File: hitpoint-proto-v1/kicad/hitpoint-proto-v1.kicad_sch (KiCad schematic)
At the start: 22 parts, among them J1 Conn_01x05_Male, J2 Conn_01x06_Female, J3 Conn_01x06_Female, J4 Conn_01x06_Female, J5 Conn_01x06_Female, U1 STM32G030Fx, U2 IRM-H6XXT

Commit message: PCB done so far
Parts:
- added C1: 100nF, Capacitor_SMD:C_0603_1608Metric, symbol Device:C
- renumbered C1 to C2, C2 to C3, C3 to C4, C4 to C5, C5 to C6, C6 to C7
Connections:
- net +3V3: now also J2.1 (Pin_1), J3.1 (Pin_1), J4.1 (Pin_1), J5.1 (Pin_1), C1.1; no longer J2.2 (Pin_2), J3.2 (Pin_2), J4.2 (Pin_2), J5.2 (Pin_2)
- net +5V: now also J2.2 (Pin_2), J3.2 (Pin_2), J4.2 (Pin_2), J5.2 (Pin_2); no longer J2.1 (Pin_1), J3.1 (Pin_1), J4.1 (Pin_1), J5.1 (Pin_1)
- net GND: now also C1.2
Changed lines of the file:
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@@
   (symbol (lib_id "Device:C") (at 137.16 66.04 0) (unit 1)
     (in_bom yes) (on_board yes)
-    (property "Reference" "C3" (id 0) (at 138.43 63.5 0)
+    (property "Reference" "C4" (id 0) (at 138.43 63.5 0)
       (effects (font (size 1.27 1.27)) (justify left))
     )
@@
   (symbol (lib_id "Device:C") (at 30.48 119.38 0) (unit 1)
     (in_bom yes) (on_board yes)
-    (property "Reference" "C1" (id 0) (at 31.75 121.92 0)
-      (effects (font (size 1.27 1.27)) (justify left))
-    )
-    (property "Value" "10uF" (id 1) (at 31.75 124.46 0)
+    (property "Reference" "C2" (id 0) (at 31.75 116.84 0)
+      (effects (font (size 1.27 1.27)) (justify left))
+    )
+    (property "Value" "10uF" (id 1) (at 31.75 121.92 0)
       (effects (font (size 1.27 1.27)) (justify left))
     )
@@
     (pin "6")
   )
-  (symbol (lib_id "power:+5V") (at 193.04 123.19 90) (unit 1)
-    (in_bom yes) (on_board yes)
-    (property "Reference" "#PWR013" (id 0) (at 196.85 123.19 0)
-      (effects (font (size 1.27 1.27)) hide)
-    )
-    (property "Value" "+5V" (id 1) (at 187.96 123.19 90))
-    (property "Footprint" "" (id 2) (at 193.04 123.19 0)
-      (effects (font (size 1.27 1.27)) hide)
-    )
-    (property "Datasheet" "" (id 3) (at 193.04 123.19 0)
-      (effects (font (size 1.27 1.27)) hide)
-    )
-    (pin "1")
-  )
   (symbol (lib_id "LED:WS2812B") (at 86.36 66.04 0) (unit 1)
     (in_bom yes) (on_board yes) (fields_autoplaced)
@@
   (symbol (lib_id "Device:C") (at 152.4 66.04 0) (unit 1)
     (in_bom yes) (on_board yes)
-    (property "Reference" "C5" (id 0) (at 153.67 63.5 0)
+    (property "Reference" "C6" (id 0) (at 153.67 63.5 0)
       (effects (font (size 1.27 1.27)) (justify left))
     )
@@
     (pin "2")
   )
+  (symbol (lib_name "+3V3_1") (lib_id "power:+3V3") (at 193.04 123.19 90) (unit 1)
+    (in_bom yes) (on_board yes) (fields_autoplaced)
+    (property "Reference" "#PWR0101" (id 0) (at 196.85 123.19 0)
+      (effects (font (size 1.27 1.27)) hide)
+    )
+    (property "Value" "+3V3" (id 1) (at 189.23 123.1899 90)
+      (effects (font (size 1.27 1.27)) (justify left))
+    )
+    (property "Footprint" "" (id 2) (at 193.04 123.19 0)
+      (effects (font (size 1.27 1.27)) hide)
+    )
+    (property "Datasheet" "" (id 3) (at 193.04 123.19 0)
+      (effects (font (size 1.27 1.27)) hide)
+    )
+    (pin "1")
+  )
   (symbol (lib_id "Device:C") (at 232.41 66.04 180) (unit 1)
     (in_bom yes) (on_board yes) (fields_autoplaced)
-    (property "Reference" "C6" (id 0) (at 236.22 64.7699 0)
+    (property "Reference" "C7" (id 0) (at 236.22 64.7699 0)
       (effects (font (size 1.27 1.27)) (justify right))
     )
@@
     (pin "2")
   )
-  (symbol (lib_name "+3V3_1") (lib_id "power:+3V3") (at 193.04 120.65 90) (unit 1)
-    (in_bom yes) (on_board yes)
-    (property "Reference" "#PWR012" (id 0) (at 196.85 120.65 0)
-      (effects (font (size 1.27 1.27)) hide)
-    )
-    (property "Value" "+3V3" (id 1) (at 187.96 120.65 90))
-    (property "Footprint" "" (id 2) (at 193.04 120.65 0)
-      (effects (font (size 1.27 1.27)) hide)
-    )
-    (property "Datasheet" "" (id 3) (at 193.04 120.65 0)
-      (effects (font (size 1.27 1.27)) hide)
-    )
-    (pin "1")
-  )
   (symbol (lib_id "Device:C") (at 144.78 66.04 0) (unit 1)
     (in_bom yes) (on_board yes)
-    (property "Reference" "C4" (id 0) (at 146.05 63.5 0)
+    (property "Reference" "C5" (id 0) (at 146.05 63.5 0)
       (effects (font (size 1.27 1.27)) (justify left))
     )
@@
   (symbol (lib_id "Device:C") (at 129.54 66.04 0) (unit 1)
     (in_bom yes) (on_board yes)
-    (property "Reference" "C2" (id 0) (at 130.81 63.5 0)
+    (property "Reference" "C3" (id 0) (at 130.81 63.5 0)
       (effects (font (size 1.27 1.27)) (justify left))
     )
@@
     (pin "6")
   )
+  (symbol (lib_id "power:+5V") (at 193.04 120.65 90) (unit 1)
+    (in_bom yes) (on_board yes) (fields_autoplaced)
+    (property "Reference" "#PWR0102" (id 0) (at 196.85 120.65 0)
+      (effects (font (size 1.27 1.27)) hide)
+    )
+    (property "Value" "+5V" (id 1) (at 189.23 120.6499 90)
+      (effects (font (size 1.27 1.27)) (justify left))
+    )
+    (property "Footprint" "" (id 2) (at 193.04 120.65 0)
+      (effects (font (size 1.27 1.27)) hide)
+    )
+    (property "Datasheet" "" (id 3) (at 193.04 120.65 0)
+      (effects (font (size 1.27 1.27)) hide)
+    )
+    (pin "1")
+  )
   (symbol (lib_id "Jumper:SolderJumper_2_Open") (at 125.73 115.57 90) (unit 1)
     (in_bom yes) (on_board yes)
@@
     )
     (pin "1")
+  )
+  (symbol (lib_id "Device:C") (at 22.86 119.38 0) (unit 1)
+    (in_bom yes) (on_board yes)
+    (property "Reference" "C1" (id 0) (at 24.13 116.84 0)
+      (effects (font (size 1.27 1.27)) (justify left))
+    )
+    (property "Value" "100nF" (id 1) (at 24.13 121.92 0)
+      (effects (font (size 1.27 1.27)) (justify left))
+    )
+    (property "Footprint" "Capacitor_SMD:C_0603_1608Metric" (id 2) (at 23.8252 123.19 0)
+      (effects (font (size 1.27 1.27)) hide)
+    )
+    (property "Datasheet" "~" (id 3) (at 22.86 119.38 0)
+      (effects (font (size 1.27 1.27)) hide)
+    )
+    (pin "1")
+    (pin "2")
   )
   (sheet_instances
@@
       (reference "#PWR011") (unit 1) (value "GND") (footprint "")
     )
-    (path "/b7a976fa-776a-4ab1-b0a2-37f6ebbf77de"
-      (reference "#PWR012") (unit 1) (value "+3V3") (footprint "")
-    )
-    (path "/956b6541-0348-4f73-b296-9061cb0e27ac"
-      (reference "#PWR013") (unit 1) (value "+5V") (footprint "")
-    )
     (path "/003fb1b7-be45-49c5-a590-681af9a34456"
       (reference "#PWR014") (unit 1) (value "GND") (footprint "")
@@
       (reference "#PWR016") (unit 1) (value "GND") (footprint "")
     )
+    (path "/a8c8ab2a-565a-403d-8f11-1f7ad63e290c"
+      (reference "#PWR0101") (unit 1) (value "+3V3") (footprint "")
+    )
+    (path "/d0ea6a16-603e-4cab-913e-14dd7c01c704"
+      (reference "#PWR0102") (unit 1) (value "+5V") (footprint "")
+    )
+    (path "/ee84faa3-67fd-47c1-8473-f69cd565e2c1"
+      (reference "C1") (unit 1) (value "100nF") (footprint "Capacitor_SMD:C_0603_1608Metric")
+    )
     (path "/5d0df2f0-223d-46e6-b5a4-c4a18f51cf9e"
-      (reference "C1") (unit 1) (value "10uF") (footprint "Capacitor_SMD:C_0805_2012Metric")
+      (reference "C2") (unit 1) (value "10uF") (footprint "Capacitor_SMD:C_0805_2012Metric")
     )
     (path "/c0eacd68-7a4c-4235-b140-b3d29b2ecb3e"
-      (reference "C2") (unit 1) (value "100nF") (footprint "Capacitor_SMD:C_0603_1608Metric")
+      (reference "C3") (unit 1) (value "100nF") (footprint "Capacitor_SMD:C_0603_1608Metric")
     )
     (path "/51436e77-e776-4180-9349-cc544ecbe37c"
-      (reference "C3") (unit 1) (value "100nF") (footprint "Capacitor_SMD:C_0603_1608Metric")
+      (reference "C4") (unit 1) (value "100nF") (footprint "Capacitor_SMD:C_0603_1608Metric")
     )
     (path "/bd03bacc-8ae0-415d-ac2b-025d5f175e5f"
-      (reference "C4") (unit 1) (value "100nF") (footprint "Capacitor_SMD:C_0603_1608Metric")
+      (reference "C5") (unit 1) (value "100nF") (footprint "Capacitor_SMD:C_0603_1608Metric")
     )
     (path "/a03d9d9a-4690-420f-a7c2-6d2e45cec7d3"
-      (reference "C5") (unit 1) (value "100nF") (footprint "Capacitor_SMD:C_0603_1608Metric")
+      (reference "C6") (unit 1) (value "100nF") (footprint "Capacitor_SMD:C_0603_1608Metric")
     )
     (path "/b169ee8a-f50b-482f-bd86-29ad5f7cd978"
-      (reference "C6") (unit 1) (value "10uF") (footprint "Capacitor_SMD:C_0805_2012Metric")
+      (reference "C7") (unit 1) (value "10uF") (footprint "Capacitor_SMD:C_0805_2012Metric")
     )
     (path "/4822abd9-c8c1-40c1-98f3-c12db2bb95bc"

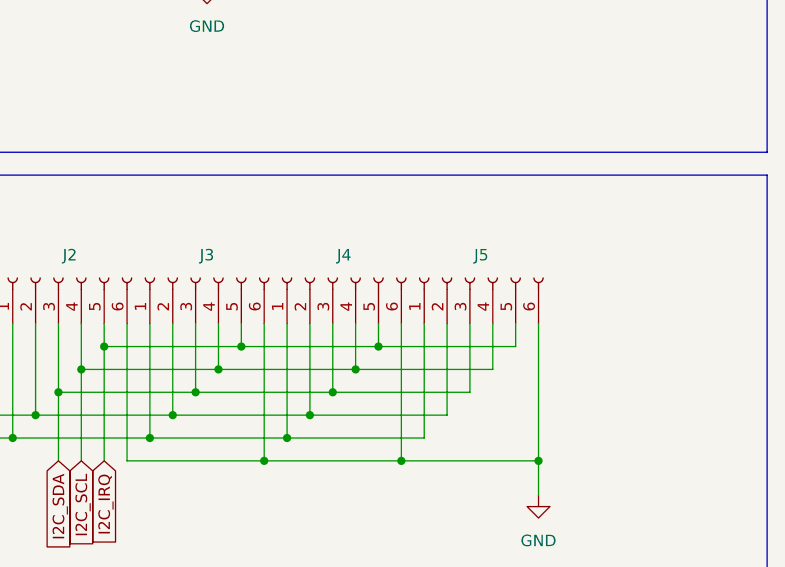
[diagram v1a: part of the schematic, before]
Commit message: Removed unused connectors from sch; added page info
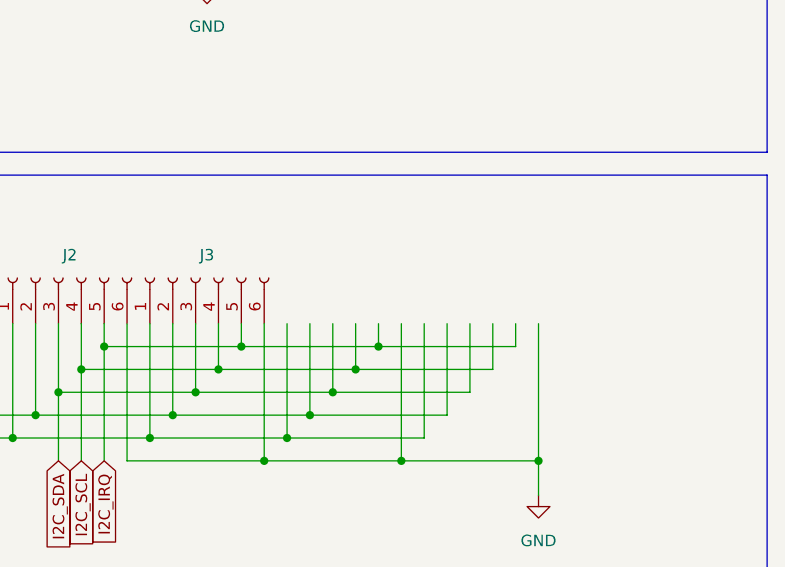
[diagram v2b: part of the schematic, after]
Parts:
- removed J4, J5: Conn_01x06_Female, Connector_PinHeader_2.54mm:PinHeader_1x06_P2.54mm_Vertical, symbol Connector:Conn_01x06_Female
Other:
- title: (none) -> Skirmish Hitpoint
